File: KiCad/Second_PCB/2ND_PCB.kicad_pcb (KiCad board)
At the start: 2 copper layers, 120 x 120 mm, 55 parts, among them J1 Conn_01x04_Pin, J2 Conn_01x04_Pin, J3 Conn_01x04_Pin

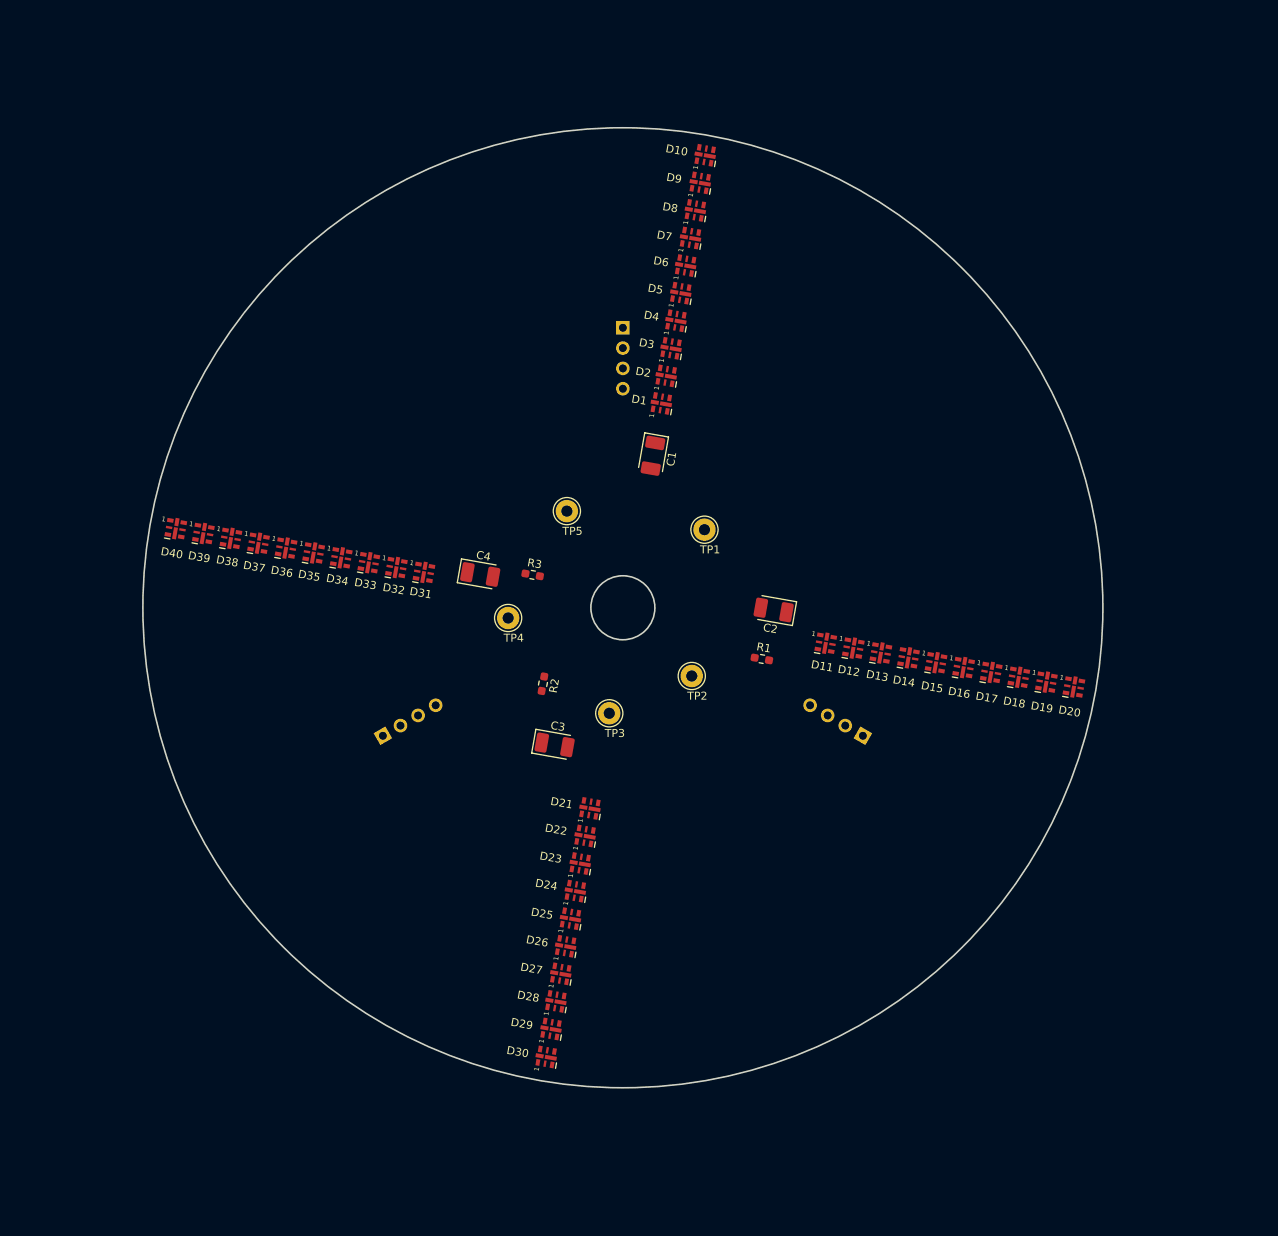
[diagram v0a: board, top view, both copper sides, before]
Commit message: added all the kicad files and gerbers of the second pcb
after sending to manufacture.
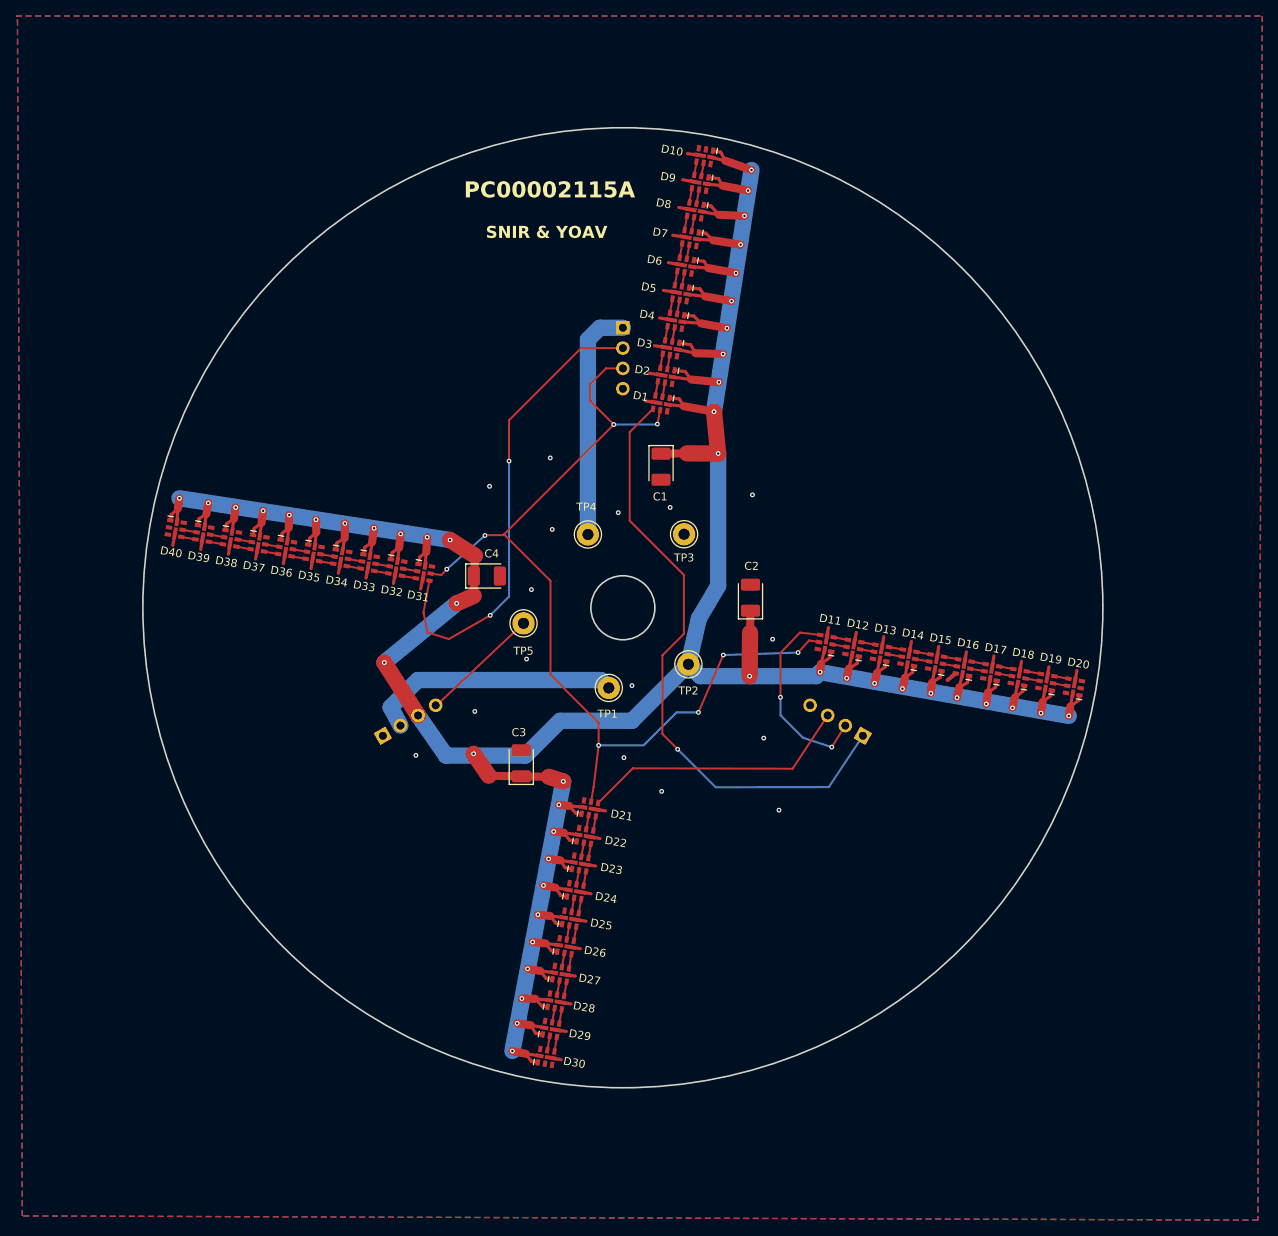
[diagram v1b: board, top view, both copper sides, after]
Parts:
- removed R1, R2, R3: 10, Resistor_SMD:R_0603_1608Metric_Pad0.98x0.95mm_HandSolder
- D1, D10, D11, D12, D13, D14, D15, D16, D17, D18, D19, D2, D20, D21, D22, D23, D24, D25, D26, D27, D28, D29, D3, D30, D31, D32, D33, D34, D35, D36, D37, D38, D39, D4, D40, D5, D6, D7, D8, D9: footprint LED_SMD:LED-APA102-2020 -> Spinning_FP:LED-APA102-2020_EDITED
- J1, J2, J3: footprint Connector_PinHeader_2.54mm:PinHeader_1x04_P2.54mm_Vertical -> Connector_PinSocket_2.54mm:PinSocket_1x04_P2.54mm_Vertical
- moved TP3 24.3 mm to (107.7, 90.8)
- moved TP1 23.1 mm to (98.2, 110.0)
- moved TP5 15.0 mm to (87.6, 102.0)
- moved TP4 14.4 mm to (95.6, 90.8)
- moved C3 4.76 mm to (87.3, 119.4), turned to 90 degrees
- moved C2 3.28 mm to (115.9, 98.7), turned to 90 degrees
- moved C1 1.70 mm to (104.8, 82.4), turned to -90 degrees
- moved TP2 1.52 mm to (108.2, 107.1)
- moved C4 0.85 mm to (83.0, 96.0), turned to 0 degrees
- moved D10 0.12 mm to (110.2, 43.5), turned to -100 degrees
- turned D1 to -100 degrees
- turned D11 to 170 degrees
- turned D12 to 170 degrees
- turned D13 to 170 degrees
- turned D14 to 170 degrees
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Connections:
- D10 pad 3: /SDO1_SDI2 -> unconnected-(D10-SDO-Pad3)
- D11 pad 4: /10_LED_ARM2/SDI -> /ESP_LEDS_SDI2
- D20 pad 3: /SDO2_SDI3 -> unconnected-(D20-SDO-Pad3)
- D21 pad 4: /10_LED_ARM3/SDI -> /ESP_LEDS_SDI3
- D30 pad 3: /SDO3_SDI4 -> unconnected-(D30-SDO-Pad3)
- D31 pad 4: /10_LED_ARM4/SDI -> /ESP_LEDS_SDI4
- D40 pad 3: /10_LED_ARM4/SDO4 -> unconnected-(D40-SDO-Pad3)
- J1 pad 1: /ESP_LEDS_CLK -> +12V
- J1 pad 2: /ESP_LEDS_SDI1 -> /ESP_LEDS_SDI4
- J1 pad 3: +3.3V -> /ESP_LEDS_CLK
- J2 pad 1: /ESP_2ND_PCB_GPIO4 -> GND
- J2 pad 2: /ESP_LEDS_SDI2 -> +3.3V
- J2 pad 4: GND -> /ESP_2ND_PCB_GPIO23
- J3 pad 1: /ESP_LEDS_SDI4 -> /ESP_LEDS_SDI1
- J3 pad 2: /ESP_LEDS_SDI3 -> /ESP_LEDS_SDI2
- J3 pad 3: +12V -> /ESP_LEDS_SDI3
- TP5 pad 1: /ESP_2ND_PCB_GPIO4 -> /ESP_2ND_PCB_GPIO23
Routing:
- net +5V: track 0.00 -> 516.4 mm, vias 0 -> 47
- net /ESP_LEDS_CLK: track 0.00 -> 121.9 mm, vias 0 -> 8
- net /ESP_LEDS_SDI1: track 0.00 -> 77.0 mm, vias 0 -> 1
- net GND: track 0.00 -> 59.3 mm, vias 0 -> 16
- net /ESP_LEDS_SDI4: track 0.00 -> 58.7 mm, vias 0 -> 2
- net /ESP_LEDS_SDI3: track 0.00 -> 34.1 mm
- net +3.3V: track 0.00 -> 31.9 mm
- net +12V: track 0.00 -> 29.3 mm
- net /ESP_LEDS_SDI2: track 0.00 -> 24.8 mm, vias 0 -> 2
- net Net-(D29-SDO): track 0.00 -> 1.85 mm
- net Net-(D29-CKO): track 0.00 -> 1.85 mm
- net Net-(D10-SDI): track 0.00 -> 1.80 mm
- net Net-(D10-CKI): track 0.00 -> 1.80 mm
- net Net-(D15-SDO): track 0.00 -> 1.80 mm
- net Net-(D38-SDO): track 0.00 -> 1.80 mm
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- added copper zone on B.Cu, net GND
- added copper zone on F.Cu, net GND
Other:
- board text added: "0.1270 mm / 0.0000 mm"
- board text added: "0.3000 mm"
- board text added: "1.6002 mm"
- board text added: "120.0025 mm x 120.0025 mm"
- board text added: "2"
- board text added: "BOARD CHARACTERISTICS"
- board text added: "Board Thickness:"
- board text added: "Board overall dimensions:"
- board text added: "Castellated pads:"
- board text added: "Copper Finish:"
- board text added: "Copper Layer Count:"
- board text added: "DIAMETER"
- board text added: "Edge card connectors:"
- board text added: "Impedance Control:"
- board text added: "Min hole diameter:"
- board text added: "Min track/spacing:"
- board text added: "No"
- board text added: "None"
- board text added: "PC00002115A"
- board text added: "Plated Board Edge:"
- board text added: "SNIR & YOAV"
- board text removed: "APA102-2020"
